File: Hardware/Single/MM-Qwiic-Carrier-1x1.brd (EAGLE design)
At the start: 109.2 x 35.6 mm, 90 parts, among them J15 MICROMOD-2222-C, J2 QWIIC_RIGHT_ANGLE, J5 Vertical Qwiic Connector, U1 MCP73831, U5 AP7361C-33FGEUDFN-8

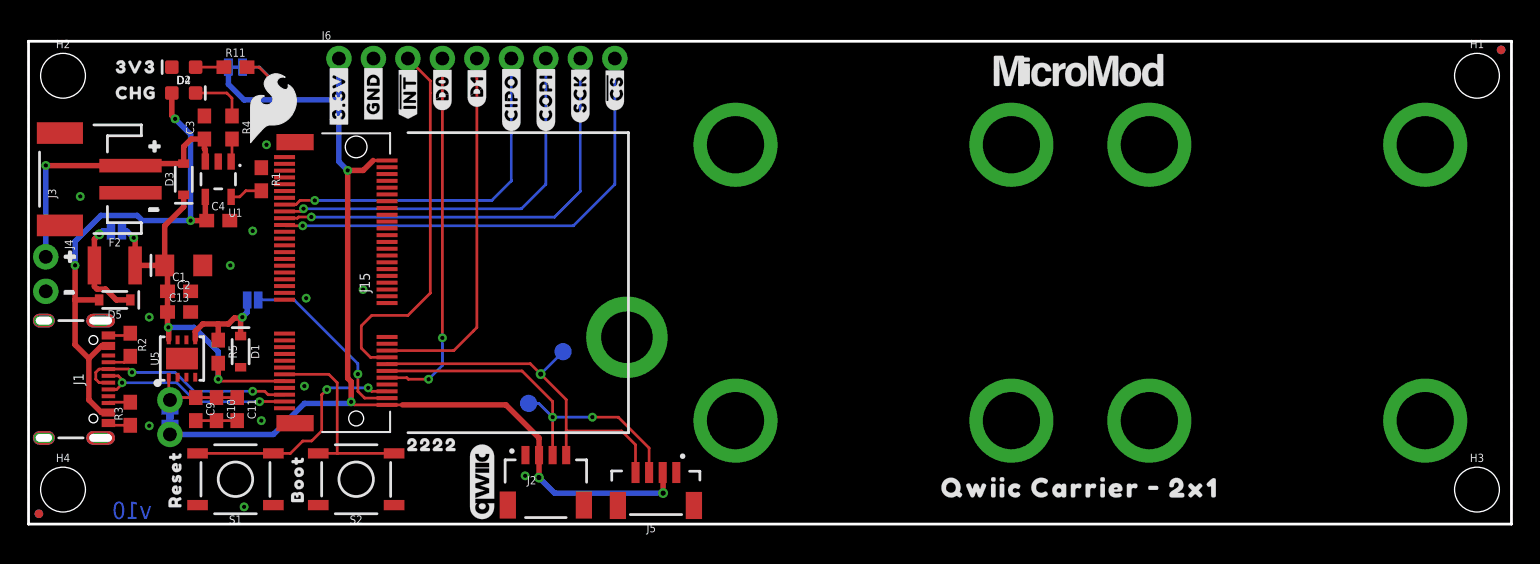
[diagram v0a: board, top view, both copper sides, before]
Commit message: Renaming
1x1 --> Single
2x1 --> Double
Re-panelized
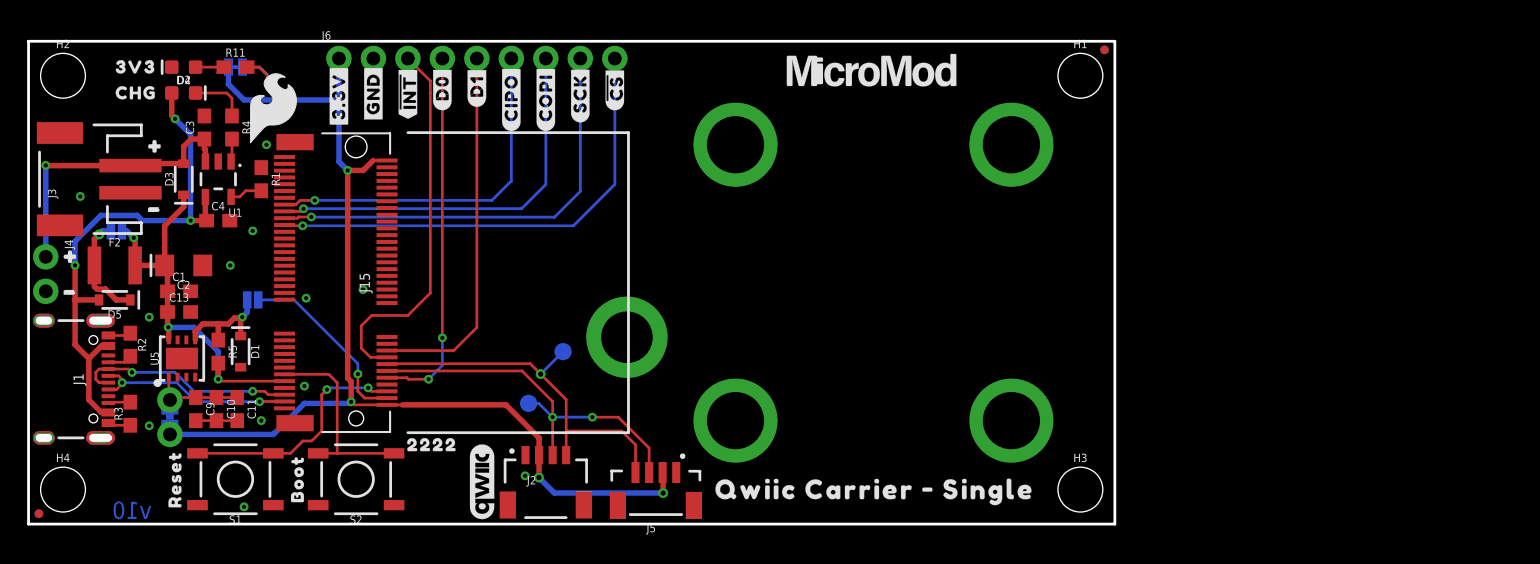
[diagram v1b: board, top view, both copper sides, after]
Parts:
- removed U$39: (no value), output:QWIIC_CARRIER_#_2X10
- U$19: device output:QWIIC_CARRIER_#_2X10 -> output:QWIIC_CARRIER_#_SINGLE0
- U$2: value QWIIC_BOARD_OUTLINESTANDOFF -> (none); device SparkFun-Boards:QWIIC_BOARD_MOUNT_SMD_STANDOFFS -> output:QWIIC_CARRIER_#_SINGLE0
- moved U$2 45.8 mm to (49.5, 2.54)
- moved H1 29.2 mm to (77.5, 33.0)
- moved H3 29.2 mm to (77.5, 2.54)
- moved FD2 29.2 mm to (79.2, 34.9)
- moved FD4 29.2 mm to (79.2, 34.9)
- moved U$19 26.1 mm to (44.6, 17.3), flipped to the bottom
- moved U$67 15.2 mm to (62.1, 33.4)
- moved LOGO1 0.51 mm to (31.8, 22.1)
- moved U$68 0.38 mm to (31.8, 19.4)
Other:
- board size 109.2 x 35.6 mm -> 80 x 35.6 mm
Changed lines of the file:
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@@
 <?xml version="1.0" encoding="utf-8"?>
 <!DOCTYPE eagle SYSTEM "eagle.dtd">
-<eagle version="9.5.2">
+<eagle version="9.6.2">
 <drawing>
 <settings>
-<setting alwaysvectorfont="no"/>
+<setting alwaysvectorfont="yes"/>
 <setting verticaltext="up"/>
 </settings>
@@
 <layer number="45" name="Holes" color="7" fill="1" visible="yes" active="yes"/>
 <layer number="46" name="Milling" color="3" fill="1" visible="no" active="yes"/>
-<layer number="47" name="Measures" color="7" fill="1" visible="yes" active="yes"/>
+<layer number="47" name="Measures" color="7" fill="1" visible="no" active="yes"/>
 <layer number="48" name="Document" color="7" fill="1" visible="no" active="yes"/>
 <layer number="49" name="Reference" color="7" fill="1" visible="no" active="yes"/>
@@
 <plain>
 <wire x1="0" y1="0" x2="0" y2="35.56" width="0.2032" layer="20"/>
-<wire x1="0" y1="35.56" x2="109.22" y2="35.56" width="0.2032" layer="20"/>
-<wire x1="109.22" y1="35.56" x2="109.22" y2="0" width="0.2032" layer="20"/>
-<wire x1="109.22" y1="0" x2="0" y2="0" width="0.2032" layer="20"/>
+<wire x1="0" y1="35.56" x2="80.01" y2="35.56" width="0.2032" layer="20"/>
+<wire x1="80.01" y1="35.56" x2="80.01" y2="0" width="0.2032" layer="20"/>
+<wire x1="80.01" y1="0" x2="0" y2="0" width="0.2032" layer="20"/>
 <text x="7.62" y="1.016" size="1.27" layer="16" font="vector" ratio="20" rot="MR180" align="center">v10</text>
 <wire x1="27.94" y1="28.829" x2="44.185" y2="28.829" width="0.2032" layer="21"/>
@@
 <wire x1="44.185" y1="6.731" x2="27.94" y2="6.731" width="0.2032" layer="21"/>
 <text x="36.83" y="-21.59" size="1.778" layer="51" font="vector" ratio="15">Priyanka Makin</text>
-<text x="58.674" y="42.418" size="1.778" layer="47" font="vector" ratio="15">in</text>
-<text x="114.554" y="23.241" size="1.778" layer="47" font="vector" ratio="15" rot="R270">in</text>
-<text x="57.404" y="46.228" size="1.778" layer="47" font="vector" ratio="15">in</text>
-<text x="118.364" y="23.241" size="1.778" layer="47" font="vector" ratio="15" rot="R270">in</text>
+<dimension x1="0" y1="35.56" x2="80.01" y2="35.56" x3="40.005" y3="45.72" textsize="1.778" textratio="15" layer="47" unit="inch"/>
+<dimension x1="80.01" y1="35.56" x2="80.01" y2="0" x3="91.44" y3="17.78" textsize="1.778" textratio="15" layer="47" unit="inch"/>
+<text x="43.434" y="42.418" size="1.778" layer="47" font="vector" ratio="15">in</text>
+<text x="85.344" y="23.241" size="1.778" layer="47" font="vector" ratio="15" rot="R270">in</text>
+<dimension x1="2.54" y1="33.02" x2="77.47" y2="33.02" x3="40.005" y3="41.91" textsize="1.778" textratio="15" layer="47" unit="inch"/>
+<dimension x1="77.47" y1="33.02" x2="77.47" y2="2.54" x3="87.63" y3="17.78" textsize="1.778" textratio="15" layer="47" unit="inch"/>
+<text x="43.434" y="46.228" size="1.778" layer="47" font="vector" ratio="15">in</text>
+<text x="89.154" y="23.241" size="1.778" layer="47" font="vector" ratio="15" rot="R270">in</text>
 <dimension x1="52.07" y1="27.94" x2="72.39" y2="27.94" x3="62.23" y3="38.1" textsize="1.778" textratio="15" layer="47" unit="inch"/>
-<text x="110.744" y="23.241" size="1.778" layer="47" font="vector" ratio="15" rot="R270">in</text>
+<dimension x1="72.39" y1="27.94" x2="72.39" y2="7.62" x3="83.82" y3="17.78" textsize="1.778" textratio="15" layer="47" unit="inch"/>
+<text x="81.534" y="23.241" size="1.778" layer="47" font="vector" ratio="15" rot="R270">in</text>
 <text x="65.024" y="38.608" size="1.778" layer="47" font="vector" ratio="15">in</text>
-<dimension x1="2.54" y1="33.02" x2="106.68" y2="33.02" x3="54.61" y3="41.91" textsize="1.778" textratio="15" layer="47" unit="inch"/>
-<dimension x1="0" y1="35.56" x2="109.22" y2="35.56" x3="54.61" y3="45.72" textsize="1.778" textratio="15" layer="47" unit="inch"/>
-<dimension x1="102.87" y1="27.94" x2="102.87" y2="7.62" x3="113.03" y3="17.78" textsize="1.778" textratio="15" layer="47" unit="inch"/>
-<dimension x1="106.68" y1="33.02" x2="106.68" y2="2.54" x3="116.84" y3="17.78" textsize="1.778" textratio="15" layer="47" unit="inch"/>
-<dimension x1="109.22" y1="35.56" x2="109.22" y2="0" x3="120.65" y3="17.78" textsize="1.778" textratio="15" layer="47" unit="inch"/>
-<dimension x1="82.55" y1="27.94" x2="102.87" y2="27.94" x3="92.71" y3="38.1" textsize="1.778" textratio="15" layer="47" unit="inch"/>
-<text x="95.504" y="38.608" size="1.778" layer="47" font="vector" ratio="15">in</text>
 </plain>
 <attributes>
@@
 </element>
 <element name="FD1" library="SparkFun-Aesthetics" package="FIDUCIAL-MICRO" value="FIDUCIALUFIDUCIAL" x="0.762" y="0.762" smashed="yes"/>
-<element name="FD2" library="SparkFun-Aesthetics" package="FIDUCIAL-MICRO" value="FIDUCIALUFIDUCIAL" x="108.458" y="34.925" smashed="yes"/>
+<element name="FD2" library="SparkFun-Aesthetics" package="FIDUCIAL-MICRO" value="FIDUCIALUFIDUCIAL" x="79.248" y="34.925" smashed="yes"/>
 <element name="FD3" library="SparkFun-Aesthetics" package="FIDUCIAL-MICRO" value="FIDUCIALUFIDUCIAL" x="0.762" y="0.762" smashed="yes" rot="MR0"/>
-<element name="FD4" library="SparkFun-Aesthetics" package="FIDUCIAL-MICRO" value="FIDUCIALUFIDUCIAL" x="108.458" y="34.925" smashed="yes" rot="MR0"/>
-<element name="H1" library="SparkFun-Hardware" package="STAND-OFF" value="STAND-OFF" x="106.68" y="33.02" smashed="yes">
-<attribute name="NAME" x="106.68" y="35.052" size="0.6096" layer="25" font="vector" ratio="20" align="bottom-center"/>
-<attribute name="VALUE" x="106.68" y="30.988" size="0.6096" layer="27" font="vector" ratio="20" align="top-center"/>
+<element name="FD4" library="SparkFun-Aesthetics" package="FIDUCIAL-MICRO" value="FIDUCIALUFIDUCIAL" x="79.248" y="34.925" smashed="yes" rot="MR0"/>
+<element name="H1" library="SparkFun-Hardware" package="STAND-OFF" value="STAND-OFF" x="77.47" y="33.02" smashed="yes">
+<attribute name="NAME" x="77.47" y="35.052" size="0.6096" layer="25" font="vector" ratio="20" align="bottom-center"/>
+<attribute name="VALUE" x="77.47" y="30.988" size="0.6096" layer="27" font="vector" ratio="20" align="top-center"/>
 </element>
 <element name="H2" library="SparkFun-Hardware" package="STAND-OFF" value="STAND-OFF" x="2.54" y="33.02" smashed="yes">
@@
 <attribute name="VALUE" x="2.54" y="30.988" size="0.6096" layer="27" font="vector" ratio="20" align="top-center"/>
 </element>
-<element name="H3" library="SparkFun-Hardware" package="STAND-OFF" value="STAND-OFF" x="106.68" y="2.54" smashed="yes">
-<attribute name="NAME" x="106.68" y="4.572" size="0.6096" layer="25" font="vector" ratio="20" align="bottom-center"/>
-<attribute name="VALUE" x="106.68" y="0.508" size="0.6096" layer="27" font="vector" ratio="20" align="top-center"/>
+<element name="H3" library="SparkFun-Hardware" package="STAND-OFF" value="STAND-OFF" x="77.47" y="2.54" smashed="yes">
+<attribute name="NAME" x="77.47" y="4.572" size="0.6096" layer="25" font="vector" ratio="20" align="bottom-center"/>
+<attribute name="VALUE" x="77.47" y="0.508" size="0.6096" layer="27" font="vector" ratio="20" align="top-center"/>
 </element>
 <element name="H4" library="SparkFun-Hardware" package="STAND-OFF" value="STAND-OFF" x="2.54" y="2.54" smashed="yes">
@@
 <attribute name="VALUE" x="23.495" y="17.78" size="0.762" layer="27" rot="R270" align="center"/>
 </element>
-<element name="LOGO1" library="SparkFun-Aesthetics" package="SFE_LOGO_NAME_FLAME_.2" value="SFE_LOGO_NAME_FLAME.2_INCH" x="31.75" y="21.59" smashed="yes" rot="MR0"/>
+<element name="LOGO1" library="SparkFun-Aesthetics" package="SFE_LOGO_NAME_FLAME_.2" value="SFE_LOGO_NAME_FLAME.2_INCH" x="31.75" y="22.098" smashed="yes" rot="MR0"/>
 <element name="U$44" library="SparkFun-Aesthetics" package="SFE_LOGO_FLAME_.2" value="" x="18.034" y="30.607" smashed="yes"/>
-<element name="U$67" library="SparkFun-MicroMod" package="MICROMOD_LOGO_.5" value="" x="77.343" y="33.401" smashed="yes"/>
-<element name="U$68" library="SparkFun-MicroMod" package="MICROMOD_LOGO_.5" value="" x="31.75" y="19.05" smashed="yes" rot="MR0"/>
+<element name="U$67" library="SparkFun-MicroMod" package="MICROMOD_LOGO_.5" value="" x="62.103" y="33.401" smashed="yes"/>
+<element name="U$68" library="SparkFun-MicroMod" package="MICROMOD_LOGO_.5" value="" x="31.75" y="19.431" smashed="yes" rot="MR0"/>
 <element name="J2" library="SparkFun-Connectors" package="JST04_1MM_RA" value="QWIIC_RIGHT_ANGLE" x="38.1" y="5.08" smashed="yes">
 <attribute name="NAME" x="36.703" y="2.921" size="0.6096" layer="25" font="vector" ratio="20"/>
@@
 <element name="U$15" library="output" package="##INT##0" value="" x="27.94" y="29.845" smashed="yes" rot="R90"/>
 <element name="U$16" library="output" package="##INT##0" value="" x="27.94" y="29.845" smashed="yes" rot="MR90"/>
-<element name="U$2" library="SparkFun-Boards" package="QWIIC_BOARD_MOUNT_SMD_STANDOFFS" value="QWIIC_BOARD_OUTLINESTANDOFF" x="92.71" y="17.78" smashed="yes"/>
-<element name="U$19" library="output" package="QWIIC_CARRIER_#_2X10" value="" x="66.167" y="2.667" smashed="yes"/>
-<element name="U$39" library="output" package="QWIIC_CARRIER_#_2X10" value="" x="42.926" y="16.51" smashed="yes" rot="MR0"/>
+<element name="U$2" library="output" package="QWIIC_CARRIER_#_SINGLE0" value="" x="49.53" y="2.54" smashed="yes"/>
+<element name="U$19" library="output" package="QWIIC_CARRIER_#_SINGLE0" value="" x="44.577" y="17.272" smashed="yes" rot="MR0"/>
 </elements>
 <signals>
@@
 <vertex x="0" y="35.56"/>
 <vertex x="0" y="0"/>
-<vertex x="109.22" y="0"/>
-<vertex x="109.22" y="35.56"/>
+<vertex x="80.01" y="0"/>
+<vertex x="80.01" y="35.56"/>
 </polygon>
 <polygon width="0.2032" layer="16" isolate="0.2032">
 <vertex x="0" y="35.56"/>
 <vertex x="0" y="0"/>
-<vertex x="109.22" y="0"/>
-<vertex x="109.22" y="35.56"/>
+<vertex x="80.01" y="0"/>
+<vertex x="80.01" y="35.56"/>
 </polygon>
 <contactref element="J2" pad="1"/>
